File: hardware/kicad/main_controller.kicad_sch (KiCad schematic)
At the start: 21 parts, among them J3 JTAG_10PIN, SW1 EN_ESP, SW2 BOOT, U6 ESP32-S3-MINI-1, Y1 32.768 kHz

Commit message: wip: revision 2
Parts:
- added R19: 5K1, Resistor_SMD:R_0402_1005Metric, symbol Device:R_Small
- added R21: 22, Resistor_SMD:R_0402_1005Metric, symbol Device:R_Small
- SW1: value EN_ESP -> RESET
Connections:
- net ESP_EN: no longer C17.1, J3.10 (~{RESET}), R14.2, SW1.2, TP6.1
- net +3.3V renamed +3V3
- net +3V3: now also R19.2
- net A7670_PWR renamed CELL_PWRKEY
- net A7670_RST renamed CELL_RESET
- net A7670_RX renamed CELL_RXD
- net A7670_STATUS renamed CELL_STATUS
- net A7670_TX renamed CELL_TXD
- net EN_GPS renamed GNSS_EN
- net EN_VBAT_CELL renamed CELL_VBAT_EN
- net ESP_32K_N: no longer names the net of C16.2, U6.20 (GPIO16/U0CTS/ADC2_CH5/XTAL_32K_N), Y1.1
- net ESP_32K_P: no longer names the net of C15.1, Y1.2
- net ESP_32K_P: now also R21.2; no longer U6.19 (GPIO15/U0RTS/ADC2_CH4/XTAL_32K_P)
- net ESP_BOOT renamed BOOT_MODE0
- net BOOT_MODE0: now also R19.1
- net GPS_HV_FO renamed GNSS_FO
- net GPS_HV_RST renamed GNSS_RESET
- net GPS_HV_RXD renamed GNSS_RXD
- net GPS_HV_TXD renamed GNSS_TXD
- net IMU_SCL renamed FG_SCL
- net IMU_SDA renamed FG_SDA
- net MAX17048_INT renamed FG_INT
- new net: R21.1, U6.19 (GPIO15/U0RTS/ADC2_CH4/XTAL_32K_P)
- new net CHIP_EN: C17.1, J3.10 (~{RESET}), R14.2, SW1.2, TP6.1
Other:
- note removed: "32.768kHz Crystal"
- moved on the sheet: C15, C16, C17, R11, R14, R15, R8, R9, SW1, SW2, TP5, TP6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

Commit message: wip: revision 2
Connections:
- net GNSS_VBCKP_EN: now reaches U6.26 (GPIO26)
- net BOOT_MODE1: now reaches U6.44 (GPIO46)
- net CELL_VBAT_EN renamed CELL_EN
- no-connect marks 14 -> 12
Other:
- note added: "Boot Button"
- note added: "JTAG Port"
- note added: "Main Controller"
- note added: "Reset Button"
- note added: "Sheets Connection"
- note removed: "EN/Reset"
- note removed: "ESP32-MINI"
- note removed: "JTAG"
- moved on the sheet: C15, C16, C17, C6, C7, J3, R11, R14, R15, R18, R19, R21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

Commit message: wip: revision 2
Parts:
- added R11: 1M, Resistor_SMD:R_0402_1005Metric, symbol Device:R_Small
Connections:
- net +3V3: now also R11.1
- net GNSS_SDBY: now reaches U6.41 (GPIO45)
- net GNSS_SDBY: now also R11.2
- net FG_SCL renamed SCL
- net FG_SDA renamed SDA
- no-connect marks 12 -> 11
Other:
- moved on the sheet: C15, C16, C17, C6, C7, R11, R14, R15, R18, R19, R21, R7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

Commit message: wip: revision 2
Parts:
- R11: value 1M -> 10K
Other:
- moved on the sheet: C17, R14, R19, SW1, SW2, TP5, TP6

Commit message: wip: revision 2
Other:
- moved on the sheet: J3

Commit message: wip: revision 2
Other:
- moved on the sheet: C15, C16, C17, C6, C7, J3, R11, R14, R15, R18, R19, R21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

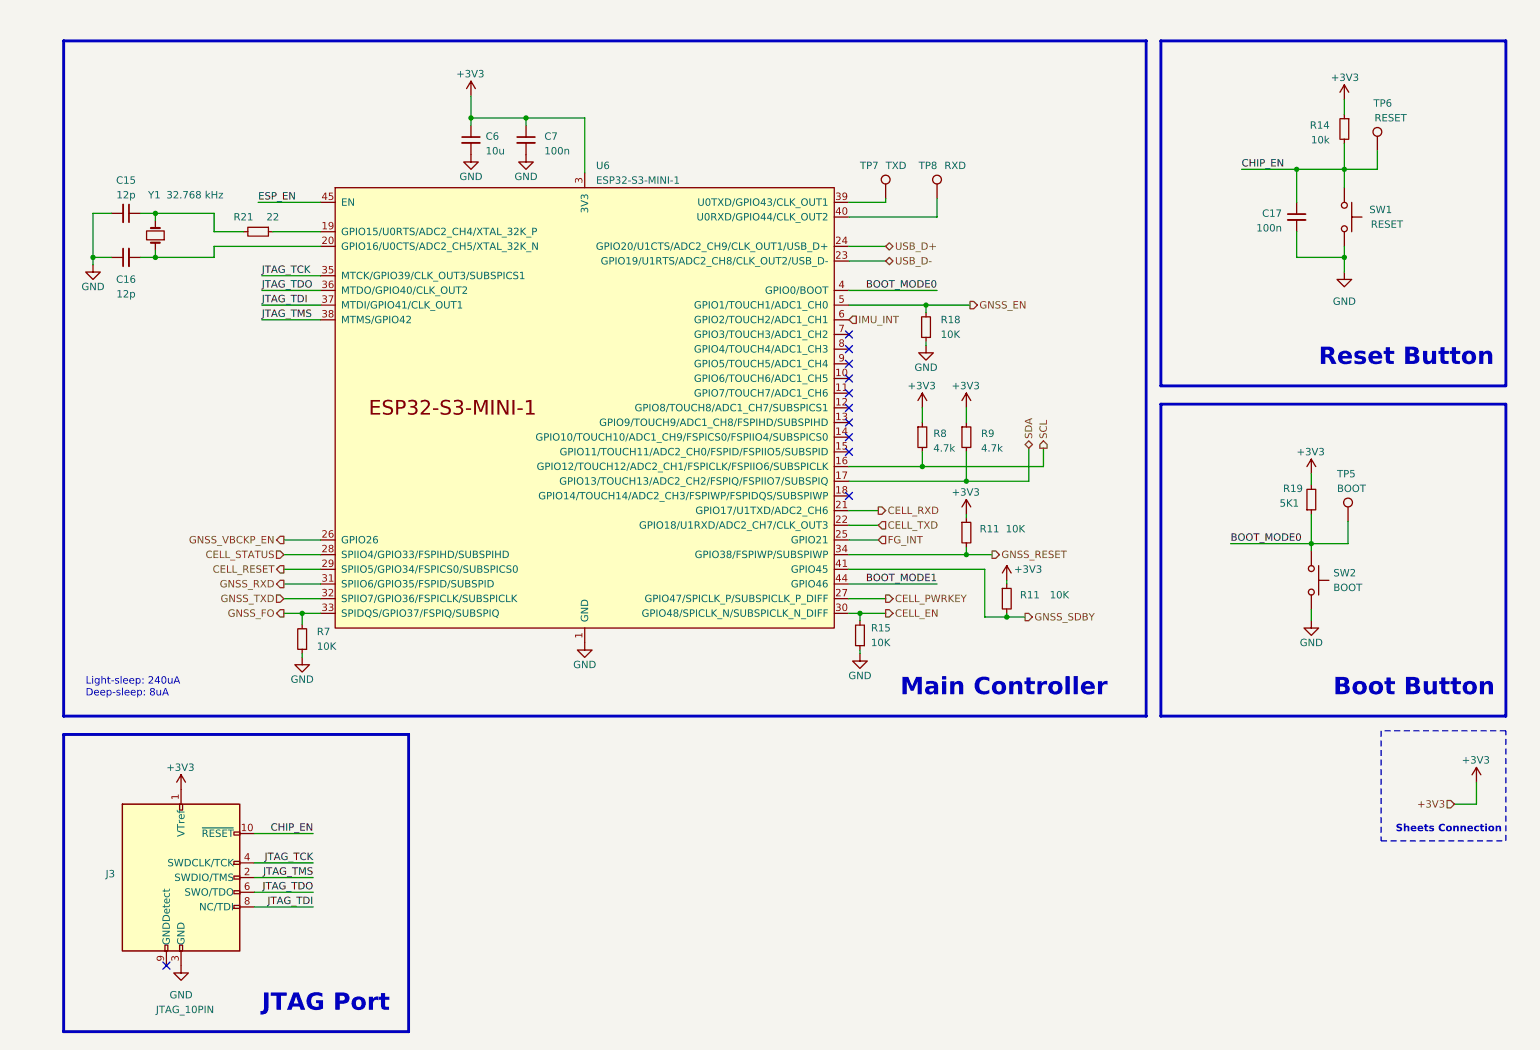
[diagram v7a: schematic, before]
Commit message: clean-up and update antenna
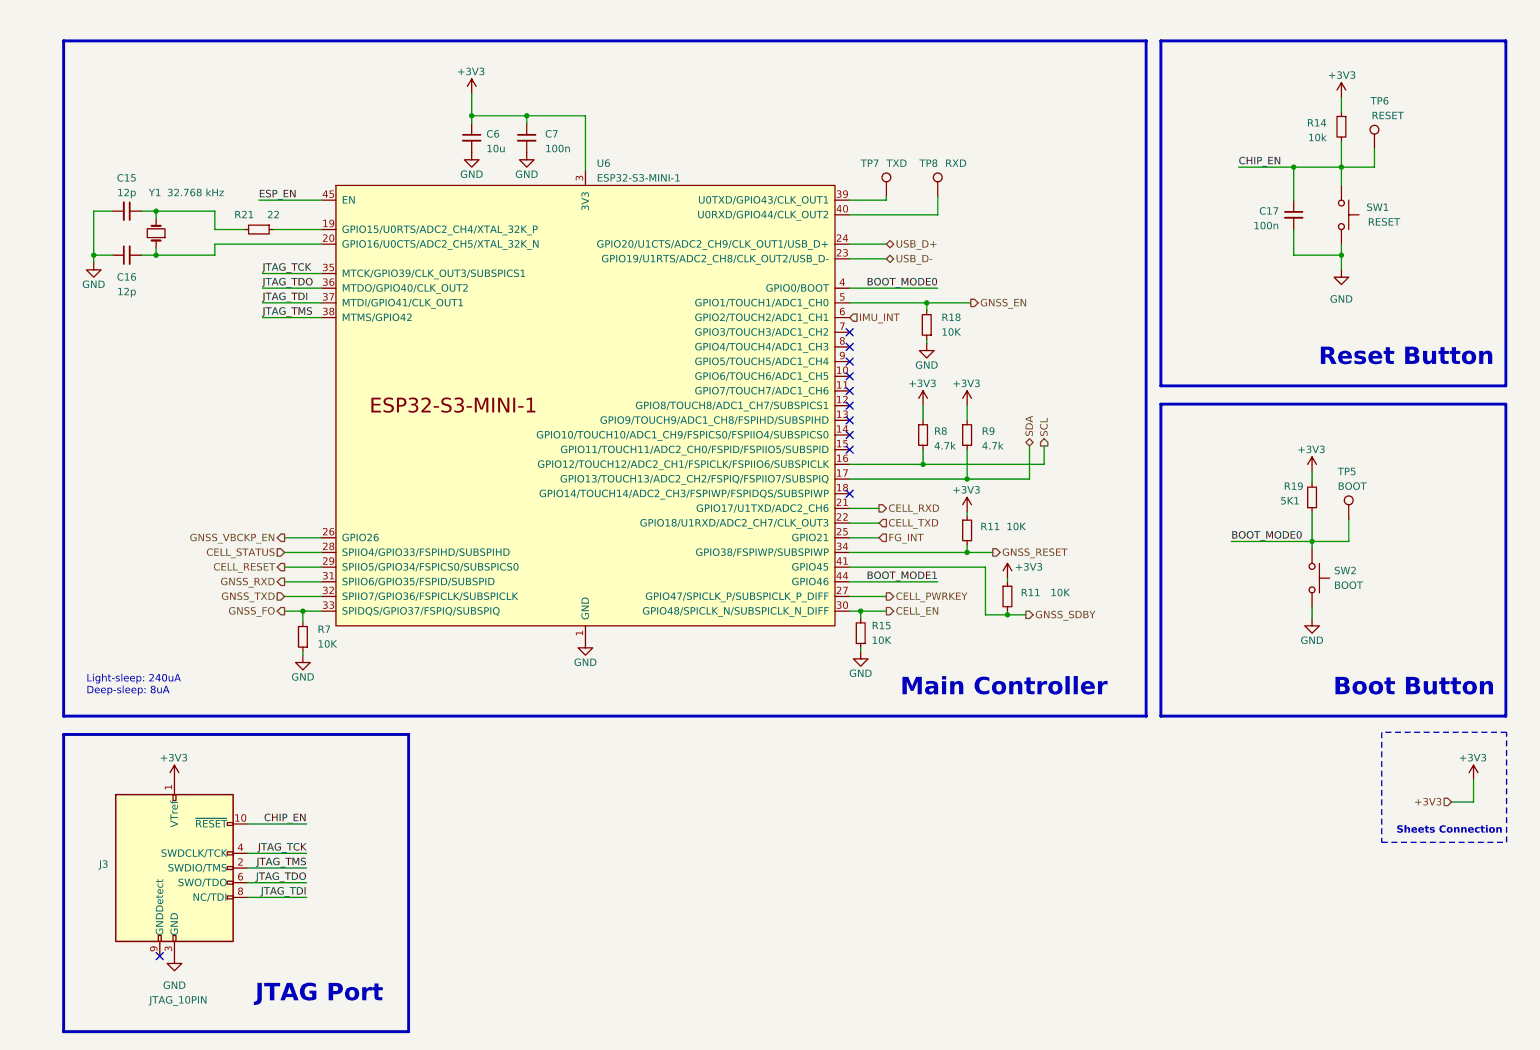
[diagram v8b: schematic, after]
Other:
- moved on the sheet: C17, J3, R14, SW1, TP6
